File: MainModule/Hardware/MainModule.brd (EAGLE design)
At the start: 123.2 x 100 mm, 19 parts, among them IC1 MC33269D-3.3, U1 ULN2803ADW, U2 ULN2803ADW, U3 ULN2803ADW, X1 MKDSN1,5/8-5,08, X2 MKDSN1,5/8-5,08, X3 MKDSN1,5/8-5,08, X4 MKDSN1,5/2-5,08, X5 MKDSN1,5/3-5,08, X6 057-016-0, X7 057-016-0

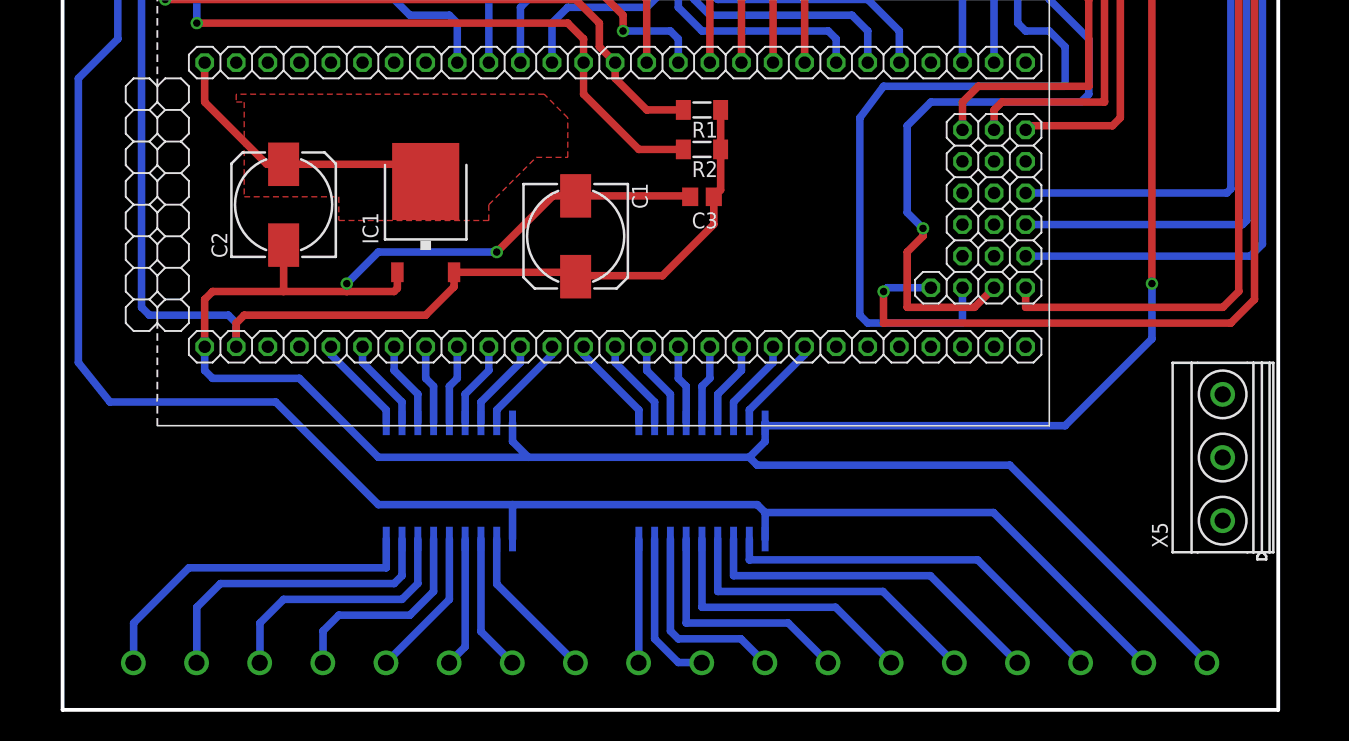
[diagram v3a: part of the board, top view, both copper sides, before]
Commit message: Reduce number of outputs and increase power of each of them.
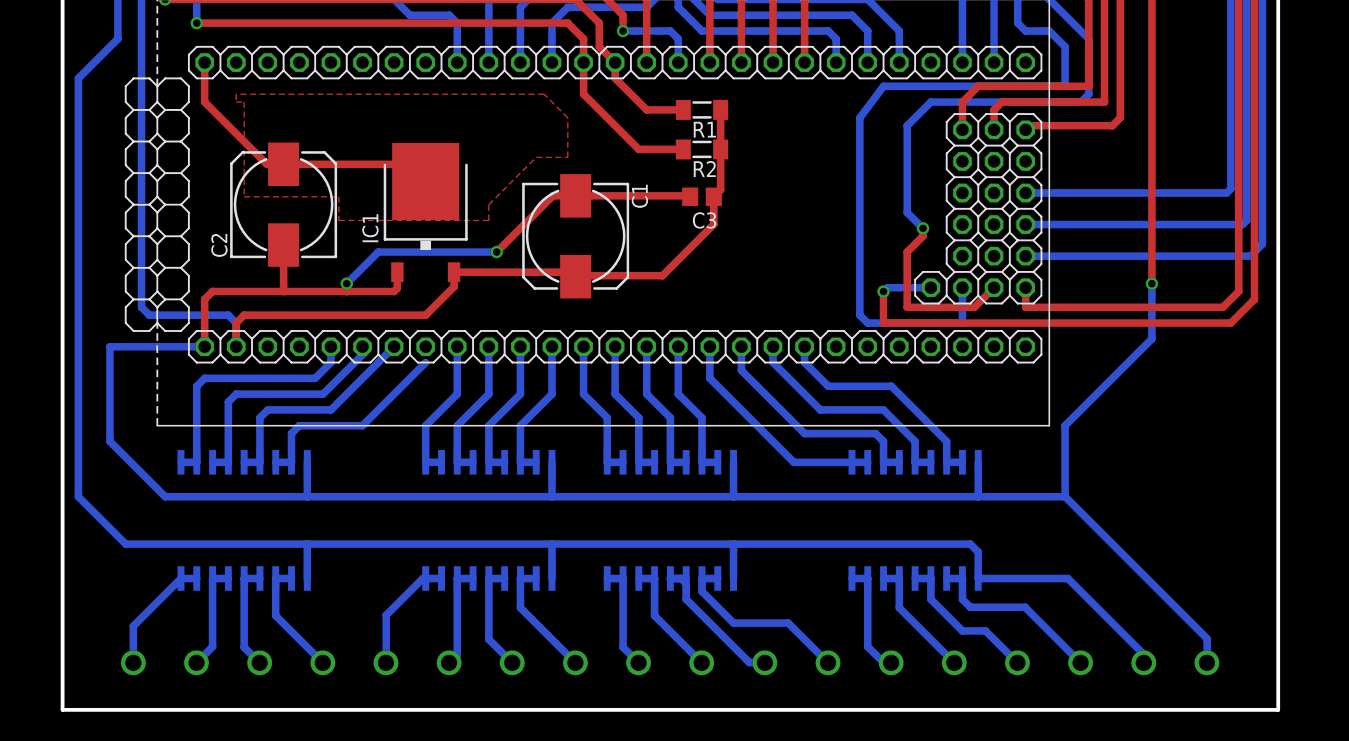
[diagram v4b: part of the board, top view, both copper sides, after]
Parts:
- removed X5: MKDSN1,5/3-5,08, con-phoenix-508:MKDSN1,5/3-5,08
- added U4, U5: ULN2803ADW, ULN2803:SOIC127P1030X265-18N
- moved U2 17.4 mm to (50.8, 19.1)
- moved U1 16.8 mm to (31.1, 19.1)
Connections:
- removed net N$35: U2.16, X2.3
- removed net N$36: U2.15, X2.4
- removed net N$37: U2.14, X2.5
- removed net N$38: U2.13, X2.6
- removed net N$39: U2.12, X2.7
- removed net N$40: U2.11, X2.8
- new net N$22: U1.15, U1.16, X1.2
- new net N$23: U1.13, U1.14, X1.3
- new net P0.25: LPC1.17, U5.1, U5.2
- new net P0.26: LPC1.18, U5.3, U5.4
- new net P1.30: LPC1.19, U5.5, U5.6
- new net P1.31: LPC1.20, U5.7, U5.8
- net GND: now also U4.9, U5.9
- net N$1: now also U1.2
- net N$10: now also U4.3, U4.4; no longer U2.2
- net N$11: now also U4.5, U4.6; no longer U2.3
- net N$12: now also U4.7, U4.8; no longer U2.4
- net N$13: now also U5.17, U5.18, X2.5; no longer LPC1.17, U2.5
- net N$14: now also U5.15, U5.16, X2.6; no longer LPC1.18, U2.6
- net N$15: now also U2.17, U2.18, X1.5; no longer LPC1.19, U2.7
- net N$16: now also U5.13, U5.14, X2.7; no longer LPC1.20, U2.8
- net N$2: now also U1.3, U1.4; no longer U1.2
- net N$25: now also U1.17
- net N$26: now also U1.11, U1.12, X1.4; no longer U1.17, X1.2
- net N$27: now also U5.11, U5.12, X2.8; no longer U1.16, X1.3
- net N$28: now also U2.15, U2.16, X1.6; no longer U1.15, X1.4
- net N$29: now also U2.13, U2.14, X1.7; no longer U1.14, X1.5
- net N$3: now also U1.5, U1.6; no longer U1.3
- net N$30: now also U2.11, U2.12, X1.8; no longer U1.13, X1.6
- net N$31: now also U4.17, U4.18, X2.1; no longer U1.12, X1.7
- net N$32: now also U4.15, U4.16, X2.2; no longer U1.11, X1.8
- net N$33: now also U4.13, U4.14, X2.3; no longer U2.18, X2.1
- net N$34: now also U4.11, U4.12, X2.4; no longer U2.17, X2.2
- net N$4: now also U1.7, U1.8; no longer U1.4
- net N$5: now also U2.1, U2.2; no longer U1.5
- net N$6: now also U2.3, U2.4; no longer U1.6
- net N$7: now also U2.5, U2.6; no longer U1.7
- net N$8: now also U2.7, U2.8; no longer U1.8
- net N$9: now also U4.1, U4.2; no longer U2.1
- net V_H: now also U4.10, U5.10
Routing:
- net N$40: track 31.8 -> 0.00 mm
- net N$39: track 28.7 -> 0.00 mm
- net N$38: track 25.6 -> 0.00 mm
- net N$37: track 22.6 -> 0.00 mm
- net N$36: track 19.5 -> 0.00 mm
- net P0.26: track 0.00 -> 18.6 mm
- net P1.31: track 0.00 -> 18.3 mm
- net P1.30: track 0.00 -> 18.3 mm
- net N$25: track 27.7 -> 9.64 mm
- net P0.25: track 0.00 -> 18.0 mm
- net N$35: track 16.1 -> 0.00 mm
- net N$26: track 25.0 -> 9.62 mm
- net N$1: track 7.96 -> 20.2 mm
- net N$2: track 7.44 -> 19.1 mm
- net V_H: track 184.7 -> 195.9 mm
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
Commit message: Zgolemuvanje na vodovit na izleznata strana
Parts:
- moved U5 16.9 mm to (68.6, 15.2)
- moved X4 16.9 mm to (89.5, 3.81)
- moved LPC1 16.9 mm to (32.4, 40.0)
- moved U3 16.9 mm to (50.8, 66.0)
- moved X1 16.9 mm to (23.5, 3.81)
- moved C2 16.9 mm to (17.8, 40.6)
- moved R3 16.9 mm to (18.4, 63.5)
- moved U1 16.9 mm to (14.6, 15.2)
- moved U2 16.9 mm to (34.3, 15.2)
- moved U4 16.9 mm to (48.9, 15.2)
- moved X3 16.9 mm to (48.9, 78.7)
- moved X6 16.9 mm to (14.6, 76.8)
- moved C1 16.9 mm to (41.3, 38.1)
- moved IC1 16.9 mm to (29.2, 40.0)
- moved R4 16.9 mm to (31.8, 58.4)
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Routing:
- net V_H: track 195.9 -> 201.1 mm
- net GND: track 331.9 -> 336.0 mm
- net N$15: track 9.51 -> 12.2 mm
- net N$33: track 12.4 -> 14.6 mm
- net N$34: track 14.8 -> 17.0 mm
- net N$14: track 9.88 -> 11.8 mm
- net N$16: track 12.0 -> 13.6 mm
- net N$31: track 8.57 -> 9.79 mm
- net N$27: track 14.6 -> 15.8 mm
- net N$22: track 8.59 -> 9.81 mm
- net N$25: track 9.64 -> 10.9 mm
- net N$28: track 8.32 -> 9.54 mm
- net N$32: track 9.62 -> 10.8 mm
- net N$13: track 9.18 -> 10.1 mm
- net N$26: track 9.62 -> 10.3 mm
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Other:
- outline, holes or cut-outs redrawn

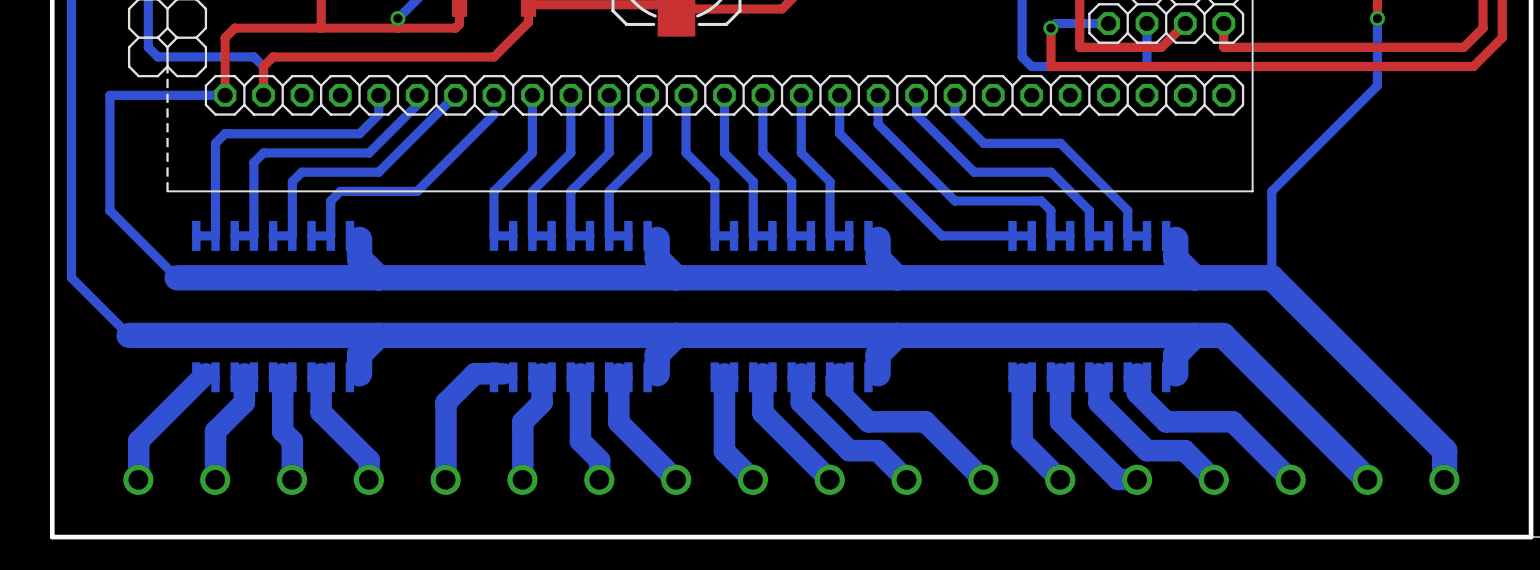
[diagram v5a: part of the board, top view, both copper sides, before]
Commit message: Dodadeni LED za signalizacija na aktiven izlez
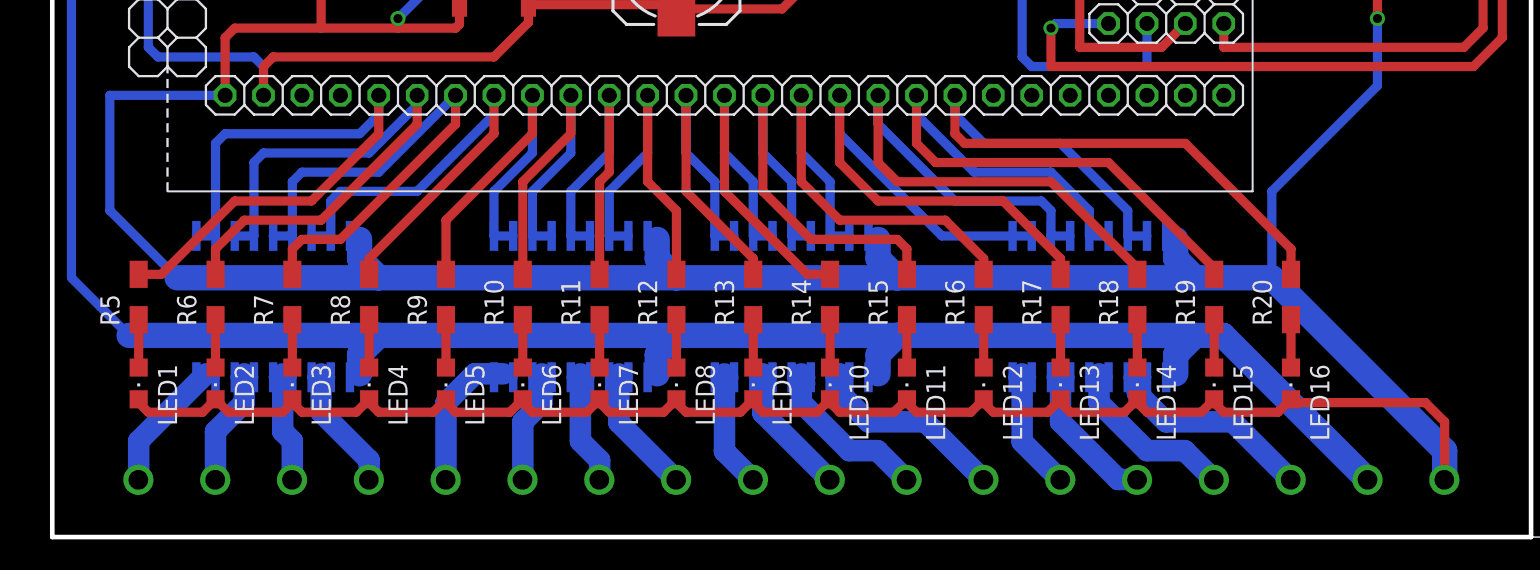
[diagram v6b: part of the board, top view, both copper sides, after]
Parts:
- added LED1, LED10, LED11, LED12, LED13, LED14, LED15, LED16, LED2, LED3, LED4, LED5, LED6, LED7, LED8, LED9: Blue, led:CHIPLED_0805
- added R10, R11, R12, R13, R14, R15, R16, R17, R18, R19, R20, R5, R6, R7, R8, R9: 133, rcl:R1206W
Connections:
- removed net N$10: LPC1.14, U4.3, U4.4
- removed net N$11: LPC1.15, U4.5, U4.6
- removed net N$12: LPC1.16, U4.7, U4.8
- removed net N$5: LPC1.9, U2.1, U2.2
- removed net N$6: LPC1.10, U2.3, U2.4
- removed net N$7: LPC1.11, U2.5, U2.6
- removed net N$8: LPC1.12, U2.7, U2.8
- removed net N$9: LPC1.13, U4.1, U4.2
- new net N$35: LED1.A, R5.1
- new net N$36: LED2.A, R6.1
- new net N$37: LED3.A, R7.1
- new net N$38: LED4.A, R8.1
- new net N$39: LED5.A, R9.1
- new net N$40: LED6.A, R10.1
- new net N$58: LED7.A, R11.1
- new net N$59: LED8.A, R12.1
- new net N$61: LED9.A, R13.1
- new net N$67: LED10.A, R14.1
- new net N$70: LED11.A, R15.1
- new net N$71: LED12.A, R16.1
- new net OUT1: LPC1.5, R5.2, U1.1, U1.2
- new net OUT10: LPC1.14, R14.2, U4.3, U4.4
- new net OUT11: LPC1.15, R15.2, U4.5, U4.6
- new net OUT12: LPC1.16, R16.2, U4.7, U4.8
- new net OUT2: LPC1.6, R6.2, U1.3, U1.4
- new net OUT3: LPC1.7, R7.2, U1.5, U1.6
- new net OUT4: LPC1.8, R8.2, U1.7, U1.8
- new net OUT5: LPC1.9, R9.2, U2.1, U2.2
- new net OUT6: LPC1.10, R10.2, U2.3, U2.4
- new net OUT7: LPC1.11, R11.2, U2.5, U2.6
- new net OUT8: LPC1.12, R12.2, U2.7, U2.8
- new net OUT9: LPC1.13, R13.2, U4.1, U4.2
- net GND: now also LED1.C, LED10.C, LED11.C, LED12.C, LED13.C, LED14.C, LED15.C, LED16.C, LED2.C, LED3.C, LED4.C, LED5.C, LED6.C, LED7.C, LED8.C, LED9.C
- net N$1: now also LED15.A, R19.1; no longer LPC1.5, U1.1, U1.2
- net N$2: now also LED13.A, R17.1; no longer LPC1.6, U1.3, U1.4
- net N$3: now also LED14.A, R18.1; no longer LPC1.7, U1.5, U1.6
- net N$4: now also LED16.A, R20.1; no longer LPC1.8, U1.7, U1.8
- net P0.25: now also R17.2
- net P0.26: now also R18.2
- net P1.30: now also R19.2
- net P1.31: now also R20.2
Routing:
- net GND: track 336.0 -> 439.1 mm
- net OUT1: track 0.00 -> 42.5 mm
- net OUT2: track 0.00 -> 39.5 mm
- net OUT3: track 0.00 -> 35.8 mm
- net OUT12: track 0.00 -> 32.3 mm
- net OUT4: track 0.00 -> 32.0 mm
- net OUT11: track 0.00 -> 30.5 mm
- net P1.31: track 18.3 -> 47.9 mm
- net OUT10: track 0.00 -> 27.0 mm
- net P1.30: track 18.3 -> 45.0 mm
- net OUT5: track 0.00 -> 25.8 mm
- net OUT9: track 0.00 -> 25.0 mm
- net P0.26: track 18.6 -> 43.5 mm
- net OUT6: track 0.00 -> 24.8 mm
- net OUT8: track 0.00 -> 24.2 mm
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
